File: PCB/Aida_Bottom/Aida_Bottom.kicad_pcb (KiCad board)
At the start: 2 copper layers, 119.7 x 83.3 mm, 129 parts, among them J1 AudioJack4, J11 Conn_01x04_Pin, J13 Conn_01x04_Pin, J15 Conn_01x04_Pin, J17 Conn_02x02_Odd_Even, J19 Conn_01x04_Pin, J20 Conn_01x06_Pin, J23 Conn_01x02_Pin, J3 USB_C_Receptacle_L, J5 Conn_01x02_Pin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

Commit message: ボトムプレート、一旦完成。
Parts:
- added ?: , clipboard:01c0b758-eab9-49d5-ba9f-7a87ce9b0684, F.Cu at (63.7, 172.9)
- moved Y1 0.97 mm to (118.3, 55.2)
- moved R15 0.72 mm to (118.0, 53.5)
- moved C23 0.70 mm to (114.9, 55.4)
- moved C6 0.70 mm to (115.9, 55.4)
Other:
- outline, holes or cut-outs redrawn

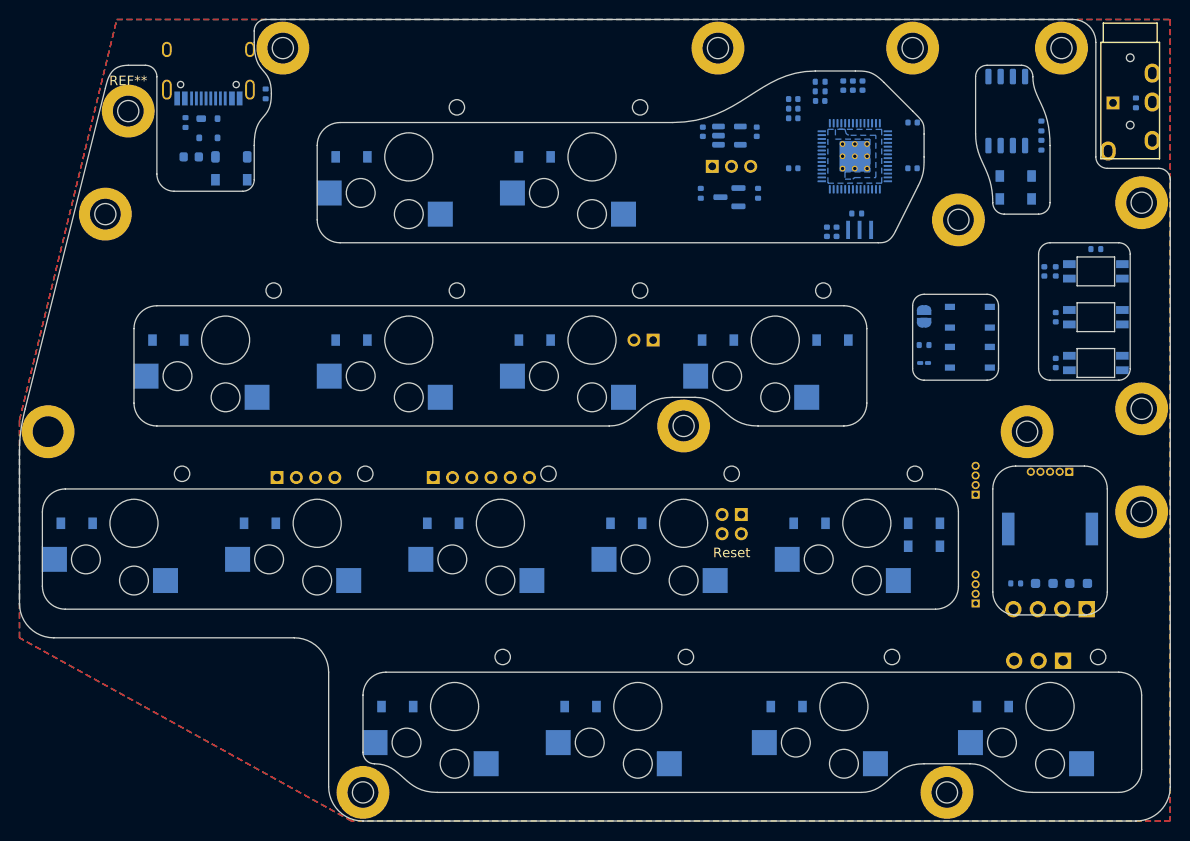
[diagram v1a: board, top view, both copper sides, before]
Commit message: 基板Baseのパーツ位置変更に合わせて、プレートの穴を再調整。
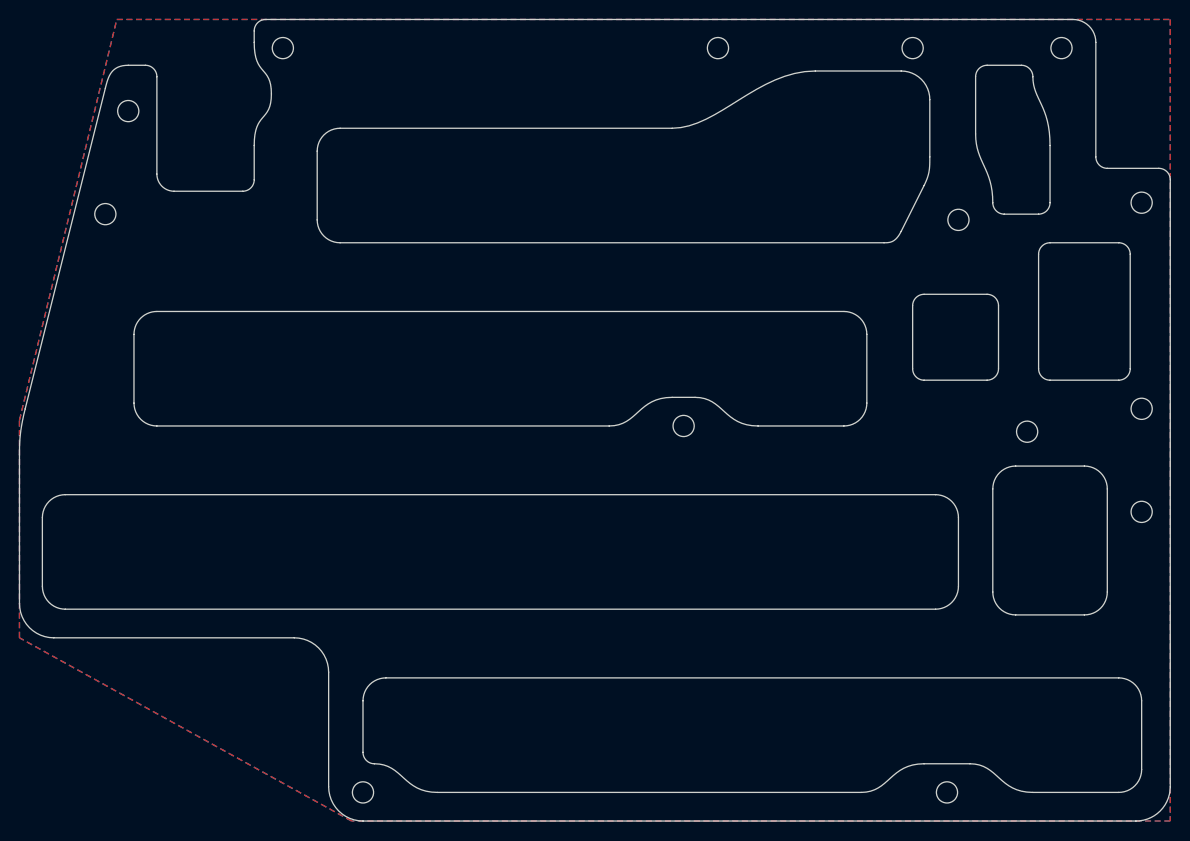
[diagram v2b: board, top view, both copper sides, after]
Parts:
- removed the ? at (63.7, 172.9)
- removed the ? at (162.7, -97.3)
- removed C1, C2: 10u, Capacitor_SMD:C_0402_1005Metric
- removed C10, C11, C12, C22, C23, C32, C33, C34, C5, C6, C7, C8, C9: 100n, Capacitor_SMD:C_0402_1005Metric
- removed C27, C28: 1u, Capacitor_SMD:C_0402_1005Metric
- removed C31: 4.7u, Capacitor_SMD:C_0402_1005Metric
- removed D1, D13, D14, D15, D16, D17, D2, D23, D24, D25, D26, D27, D28, D3, D35, D36, D37, D38, D4, D45, D5: D, Lib_Local:D_SOD-123_Emphasized_Direction_Line
- removed D43: PRTR5V0U2X, Package_TO_SOT_SMD:SOT-143
- removed F1: Fuse, Fuse:Fuse_0603_1608Metric
- removed H1: COL_L_0_from_Mid_Outside, Lib_Local:MountingHole_M2_Through-hole_tap_THC-0.8-2.0-2_minimal
- removed H13: COL_L_4_from_Mid_Inside, Lib_Local:MountingHole_M2_Through-hole_tap_THC-0.8-2.0-2_minimal
- removed H15: COL_L_4_to_Mid_Inside, Lib_Local:MountingHole_M2_Through-hole_tap_THC-0.8-2.0-2_minimal
- removed H17: COL_L_5_from_Mid_Inside, Lib_Local:MountingHole_M2_Through-hole_tap_THC-0.8-2.0-2_minimal
- removed H19: COL_L_5_to_Mid_Inside, Lib_Local:MountingHole_M2_Through-hole_tap_THC-0.8-2.0-2_minimal
- removed H2: COL_L_3_from_Mid_Inside, Lib_Local:MountingHole_M2_Through-hole_tap_THC-0.8-2.0-2_minimal
- removed H3: COL_L_4_from_Top, Lib_Local:MountingHole_M2_Through-hole_tap_THC-0.8-2.0-2_minimal
- removed H7: COL_L_0_to_Mid_Outside, Lib_Local:MountingHole_M2_Through-hole_tap_THC-0.8-2.0-2_minimal
- removed H8: COL_L_3_to_Mid_Inside, Lib_Local:MountingHole_M2_Through-hole_tap_THC-0.8-2.0-2_minimal
- removed H_btm_L3, H_btm_L4, H_btm_L5, H_btm_L6, H_mid_L1, H_mid_L2: MountingHole, Lib_Local:MountingHole_M2_Through-hole_tap_THC-0.8-1.0-2_minimal
- removed J1: AudioJack4, Lib_Local:TRRS-PJ-320A_PinNameChanged
- removed J11, J15: Conn_01x04_Pin, Connector_PinHeader_1.00mm:PinHeader_1x04_P1.00mm_Vertical
- removed J13: Conn_01x04_Pin, Connector_PinHeader_2.54mm:PinHeader_1x04_P2.54mm_Vertical
- removed J17: Conn_02x02_Odd_Even, Connector_PinHeader_2.00mm:PinHeader_2x02_P2.00mm_Vertical
- removed J19: Conn_01x04_Pin, Connector_PinHeader_2.00mm:PinHeader_1x04_P2.00mm_Vertical
- removed J20: Conn_01x06_Pin, Connector_PinHeader_2.00mm:PinHeader_1x06_P2.00mm_Vertical
- removed J23: Conn_01x02_Pin, Connector_PinHeader_2.00mm:PinHeader_1x02_P2.00mm_Vertical
- removed J3: USB_C_Receptacle_L, Connector_USB:USB_C_Receptacle_HRO_TYPE-C-31-M-12
- removed J5: Conn_01x02_Pin, Connector_PinHeader_2.00mm:PinHeader_1x03_P2.00mm_Vertical
- removed J7: Conn_01x05_Pin, Connector_PinHeader_1.00mm:PinHeader_1x05_P1.00mm_Vertical
- removed J9: Conn_01x03_Pin, Connector_PinHeader_2.54mm:PinHeader_1x03_P2.54mm_Vertical
- removed JP1: SolderJumper_2_Open, Jumper:SolderJumper-2_P1.3mm_Open_RoundedPad1.0x1.5mm
- removed L1, L2, L3: SK6812MINI-E, Lib_Local:YS-SK6812MINI-E_middle_hole_with_small_pad
- removed LS1: Speaker, Buzzer_Beeper:Buzzer_Murata_PKMCS0909E
- removed Q1: BSS138, Package_TO_SOT_SMD:SOT-23
- removed R1, R11, R12, R15, R21, R9: 1k, Resistor_SMD:R_0402_1005Metric
- removed R16, R3: 330, Resistor_SMD:R_0402_1005Metric
- removed R19: 10k, Resistor_SMD:R_0402_1005Metric
- removed R23, R25: 4.7k, Resistor_SMD:R_0603_1608Metric_Pad0.98x0.95mm_HandSolder
- removed R27, R29: 27, Resistor_SMD:R_0402_1005Metric
- removed R5, R7: 5.1k, Resistor_SMD:R_0402_1005Metric
- removed SD1: Schottky diode, Diode_SMD:D_SOD-123
- removed STLED1: LED_GREEN, LED_SMD:LED_0201_0603Metric_Pad0.64x0.40mm_HandSolder
- removed SW1: BOOT, Button_Switch_SMD:SW_SPST_PTS810
- removed SW3: RESET, Button_Switch_SMD:SW_SPST_PTS810
- removed SW_A1, SW_B1, SW_C1, SW_CMD_L1, SW_CTL1, SW_D1, SW_E1, SW_F1, SW_OPT_L1, SW_S1, SW_SPC1, SW_V1, SW_W1, SW_X1, SW_Z1: SW_Push, Lib_Local:Kailh_socket_ChocV2
- removed TP1: TestPoint, Connector_PinHeader_2.00mm:PinHeader_1x01_P2.00mm_Vertical
- removed U3: RP2040_L, Lib_Local:RP2040-QFN-56
- removed U5: W25Q128JVS, Package_SO:SOIC-8_5.3x5.3mm_P1.27mm
- removed U7: AP2112K-3.3, Package_TO_SOT_SMD:SOT-23-5
- removed Y1: 12MHz, Crystal:Resonator_SMD_Murata_CSTxExxV-3Pin_3.0x1.1mm
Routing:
- added copper zone on B.Cu, net (none)
- added copper zone on F.Cu, net (none)
- removed copper zone on B.Cu, net +1V1_L
- removed copper zone on B.Cu, net +3V3_L
- removed copper zone on B.Cu, net GND_L
- removed copper zone on F.Cu, net GND_L
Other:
- outline, holes or cut-outs redrawn
